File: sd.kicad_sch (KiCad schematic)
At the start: 40 parts, among them J2 MicroSD_1140084168, U1 USB2642_ML, Y2 ABM8G-24.000MHZ-18-D2Y-T

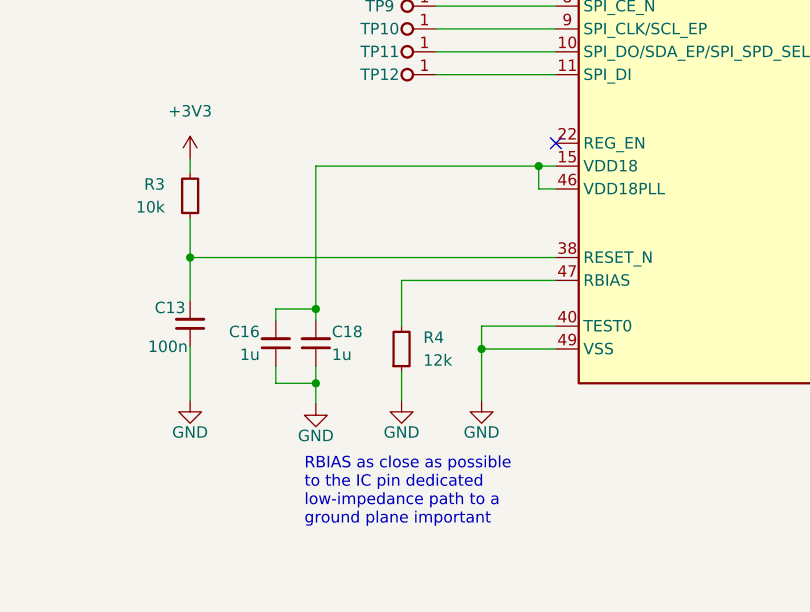
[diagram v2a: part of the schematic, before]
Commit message: [#45990] Route dif USB
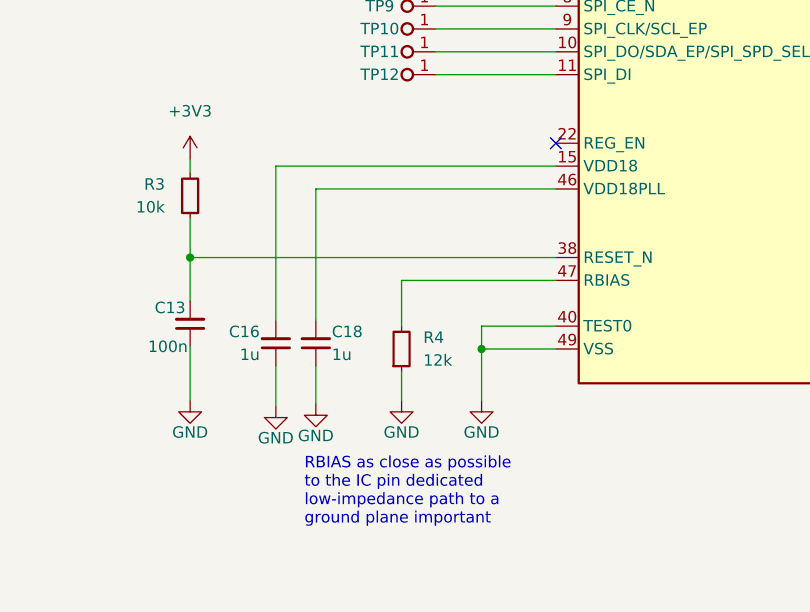
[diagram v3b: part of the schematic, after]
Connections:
- net at C16.2, U1.15 (VDD18): no longer C18.2, U1.46 (VDD18PLL)
- new net: C18.2, U1.46 (VDD18PLL)
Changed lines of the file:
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@@
   (junction (at 27.305 74.295) (diameter 0) (color 0 0 0 0)
   )
-  (junction (at 54.61 147.955) (diameter 0) (color 0 0 0 0)
-  )
   (junction (at 27.305 67.31) (diameter 0) (color 0 0 0 0)
   )
@@
   (junction (at 57.15 52.07) (diameter 0) (color 0 0 0 0)
   )
-  (junction (at 79.375 132.08) (diameter 0) (color 0 0 0 0)
-  )
   (junction (at 33.655 67.31) (diameter 0) (color 0 0 0 0)
   )
   (junction (at 257.175 53.34) (diameter 0) (color 0 0 0 0)
   )
-  (junction (at 54.61 156.21) (diameter 0) (color 0 0 0 0)
-  )
   (junction (at 20.955 74.295) (diameter 0) (color 0 0 0 0)
   )
@@
     (stroke (width 0) (type default) (color 0 0 0 0))
   )
-  (wire (pts (xy 54.61 154.305) (xy 54.61 156.21))
+  (wire (pts (xy 54.61 154.305) (xy 54.61 158.496))
     (stroke (width 0) (type default) (color 0 0 0 0))
   )
@@
     (stroke (width 0) (type default) (color 0 0 0 0))
   )
-  (wire (pts (xy 79.375 132.08) (xy 79.375 134.62))
-    (stroke (width 0) (type default) (color 0 0 0 0))
-  )
   (wire (pts (xy 130.81 109.22) (xy 153.67 109.22))
     (stroke (width 0) (type default) (color 0 0 0 0))
@@
     (stroke (width 0) (type default) (color 0 0 0 0))
   )
-  (wire (pts (xy 50.165 147.955) (xy 54.61 147.955))
-    (stroke (width 0) (type default) (color 0 0 0 0))
-  )
-  (wire (pts (xy 54.61 147.955) (xy 54.61 149.225))
-    (stroke (width 0) (type default) (color 0 0 0 0))
-  )
-  (wire (pts (xy 79.375 134.62) (xy 81.28 134.62))
+  (wire (pts (xy 54.61 134.62) (xy 81.28 134.62))
     (stroke (width 0) (type default) (color 0 0 0 0))
   )
@@
     (stroke (width 0) (type default) (color 0 0 0 0))
   )
+  (wire (pts (xy 54.61 149.225) (xy 54.61 134.62))
+    (stroke (width 0) (type default) (color 0 0 0 0))
+  )
   (wire (pts (xy 241.935 55.88) (xy 250.825 55.88))
     (stroke (width 0) (type default) (color 0 0 0 0))
@@
     (stroke (width 0) (type default) (color 0 0 0 0))
   )
-  (wire (pts (xy 54.61 156.21) (xy 54.61 158.496))
-    (stroke (width 0) (type default) (color 0 0 0 0))
-  )
   (wire (pts (xy 234.569 62.738) (xy 234.569 64.643))
     (stroke (width 0) (type default) (color 0 0 0 0))
@@
     (stroke (width 0) (type default) (color 0 0 0 0))
   )
-  (wire (pts (xy 79.375 132.08) (xy 81.28 132.08))
+  (wire (pts (xy 50.165 132.08) (xy 81.28 132.08))
     (stroke (width 0) (type default) (color 0 0 0 0))
   )
@@
     (stroke (width 0) (type default) (color 0 0 0 0))
   )
-  (wire (pts (xy 50.165 154.305) (xy 50.165 156.21))
+  (wire (pts (xy 50.165 154.305) (xy 50.165 158.75))
     (stroke (width 0) (type default) (color 0 0 0 0))
   )
@@
     (stroke (width 0) (type default) (color 0 0 0 0))
   )
-  (wire (pts (xy 50.165 156.21) (xy 54.61 156.21))
-    (stroke (width 0) (type default) (color 0 0 0 0))
-  )
   (polyline (pts (xy 191.135 76.835) (xy 286.385 76.835))
     (stroke (width 0) (type default) (color 0 0 0 0))
@@
     (stroke (width 0) (type default) (color 0 0 0 0))
   )
-  (wire (pts (xy 54.61 147.955) (xy 54.61 132.08))
-    (stroke (width 0) (type default) (color 0 0 0 0))
-  )
   (wire (pts (xy 67.945 106.68) (xy 81.28 106.68))
     (stroke (width 0) (type default) (color 0 0 0 0))
@@
     (stroke (width 0) (type default) (color 0 0 0 0))
   )
-  (wire (pts (xy 54.61 132.08) (xy 79.375 132.08))
-    (stroke (width 0) (type default) (color 0 0 0 0))
-  )
   (wire (pts (xy 32.385 57.785) (xy 32.385 59.055))
     (stroke (width 0) (type default) (color 0 0 0 0))
@@
     (stroke (width 0) (type default) (color 0 0 0 0))
   )
-  (wire (pts (xy 50.165 149.225) (xy 50.165 147.955))
+  (wire (pts (xy 50.165 132.08) (xy 50.165 149.225))
     (stroke (width 0) (type default) (color 0 0 0 0))
   )
@@
     (pin "2")
   )
+  (symbol (lib_id "antmicropower:GND") (at 50.165 158.75 0) (unit 1)
+    (in_bom yes) (on_board yes)
+    (property "Reference" "#PWR?" (id 0) (at 50.165 165.1 0)
+      (effects (font (size 1.27 1.27)) hide)
+    )
+    (property "Value" "GND" (id 1) (at 50.165 162.306 0))
+    (property "Footprint" "" (id 2) (at 50.165 158.75 0)
+      (effects (font (size 1.27 1.27)) hide)
+    )
+    (property "Datasheet" "" (id 3) (at 50.165 158.75 0)
+      (effects (font (size 1.27 1.27)) hide)
+    )
+    (pin "1")
+  )
   (symbol (lib_id "antmicroResistors0402:R_4k7_0402") (at 172.72 96.52 90) (unit 1)

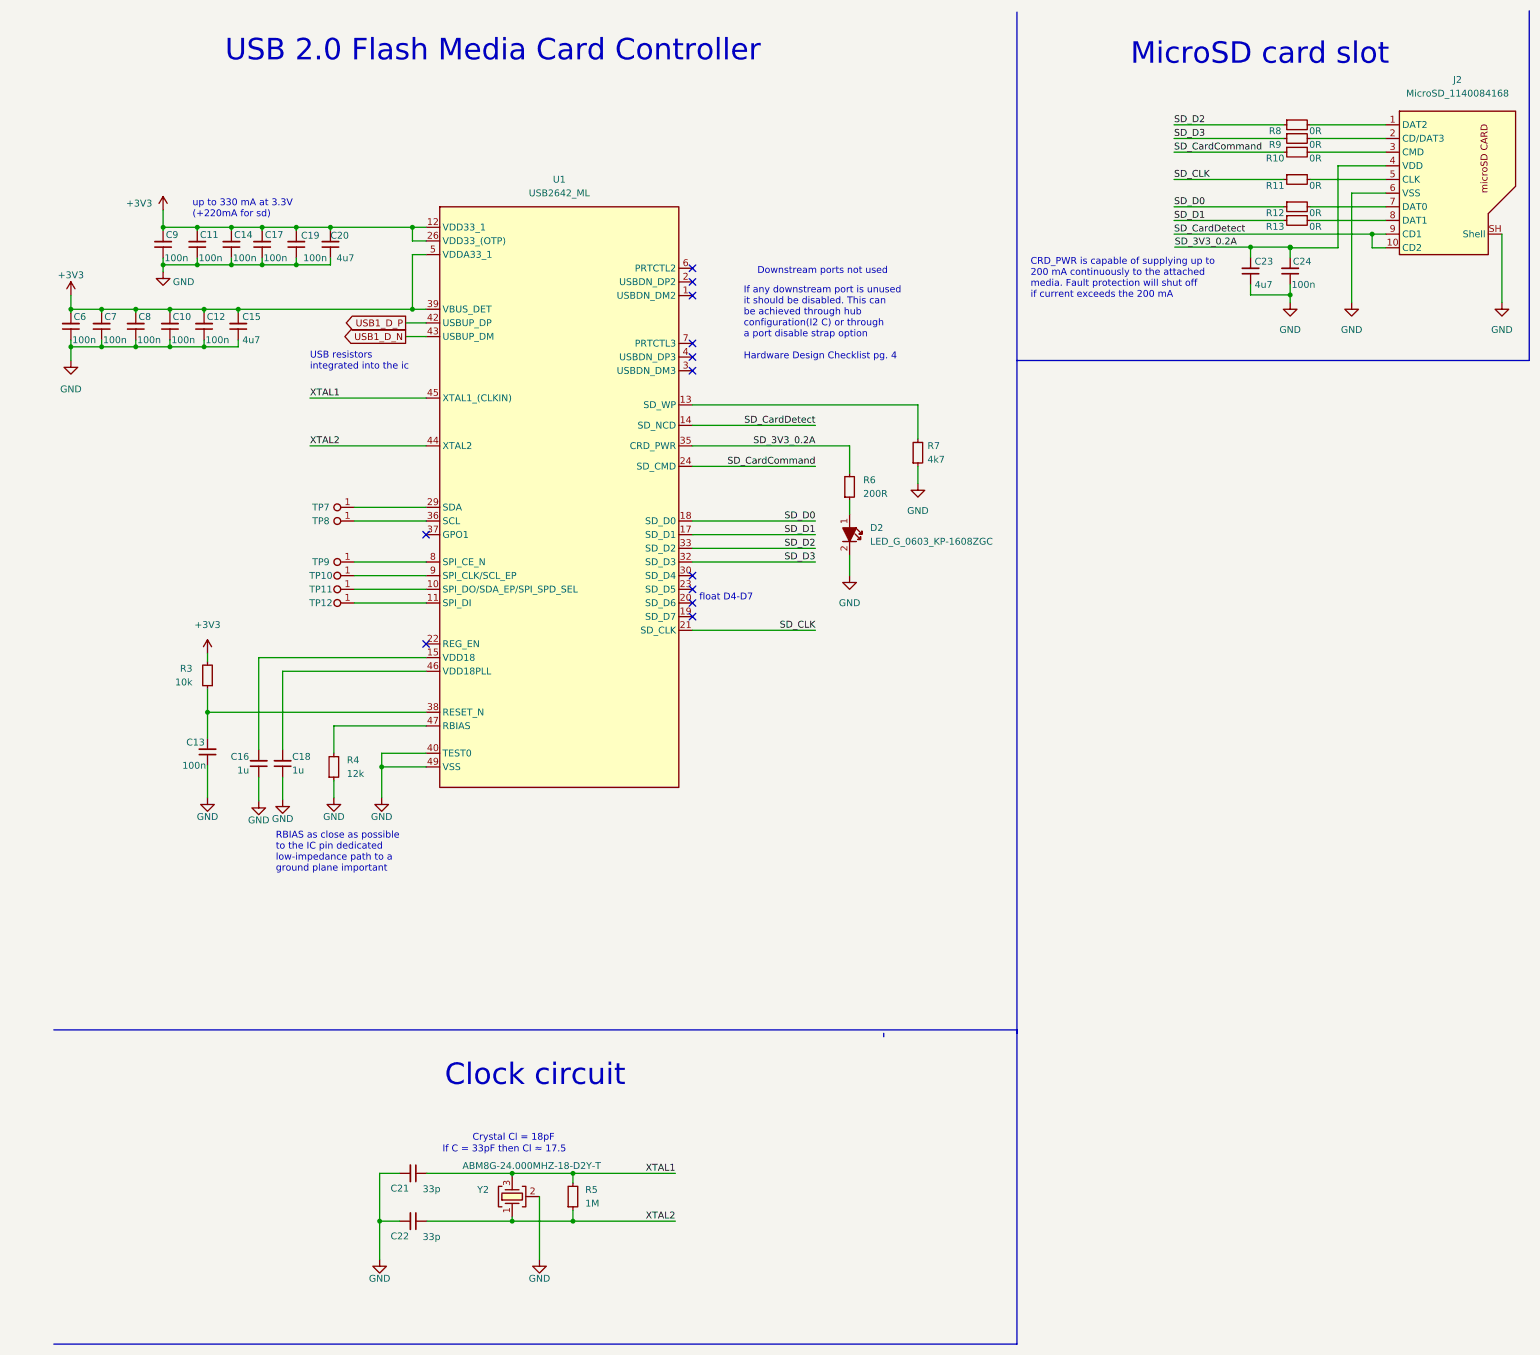
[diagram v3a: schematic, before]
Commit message: [#45990] Cosmetic changes for schematic, expand README
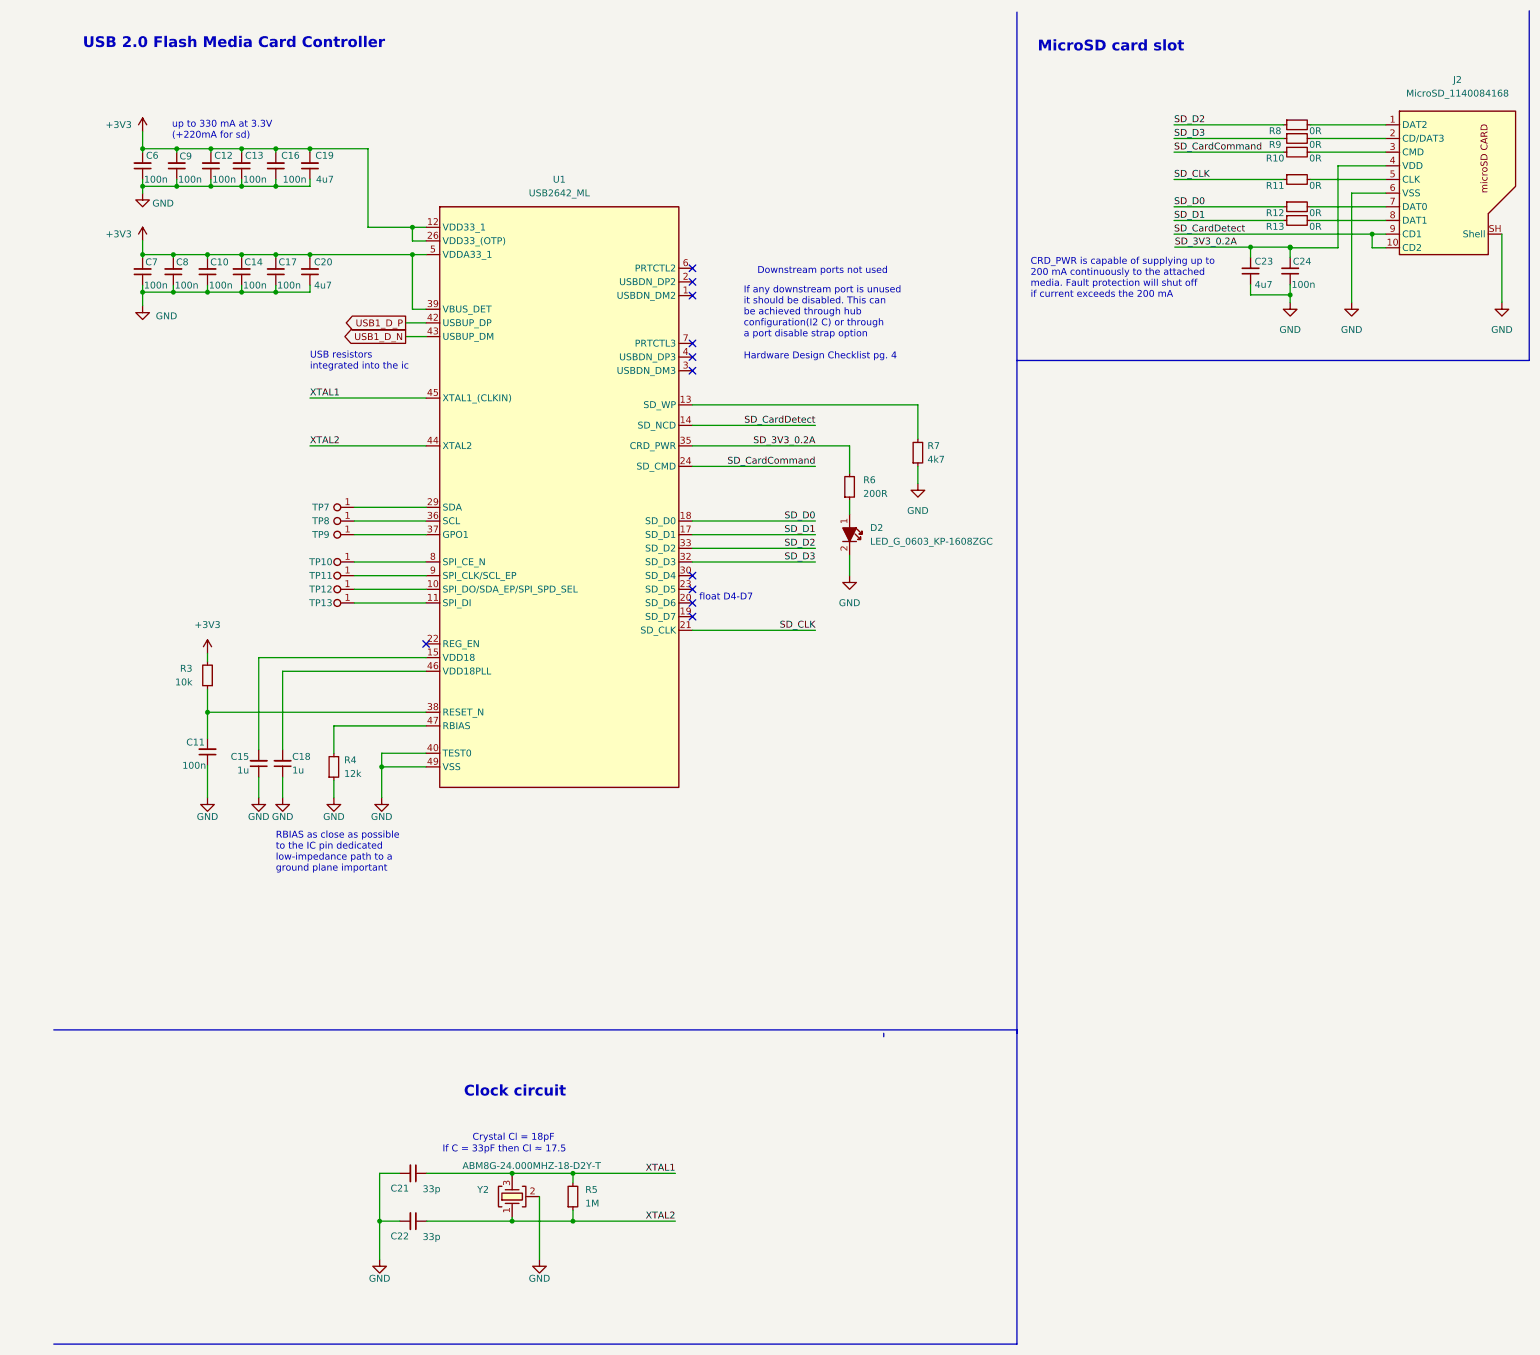
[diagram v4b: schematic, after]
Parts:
- removed R4: R_12k_0805, antmicro-footprints:R_0805_2012Metric, symbol antmicroResistorsmisc:R_12k_0805
- added R4: R_12k_0402, antmicro-footprints:R_0402_1005Metric, symbol antmicroResistors0402:R_12k_0402
- added TP9: TP_0.75mm_SMD, antmicro-footprints:TP_SMD_0.75mm, symbol antmicroTestPoints:TP_0.75mm_SMD
- renumbered C8 to C10, C13 to C11, C14 to C12, C17 to C13, C10 to C14, C16 to C15, C19 to C16, C12 to C17, C20 to C19, C15 to C20, C9 to C6, C6 to C7, C7 to C8, C11 to C9, TP9 to TP10, TP10 to TP11, TP11 to TP12, TP12 to TP13
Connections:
- net GND: now also R4.1
- net at U1.37 (GPO1): now also TP9.1
- net at U1.47 (RBIAS): now also R4.2
- no-connect marks 12 -> 11
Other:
- moved on the sheet: C10, C12, C13, C14, C16, C17, C19, C20, C6, C7, C8, C9
